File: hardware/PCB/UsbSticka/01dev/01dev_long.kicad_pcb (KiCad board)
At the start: 2 copper layers, 17.7 x 51.8 mm, 22 parts, among them P1 USB_B, P2 MIC, SW1 SW_PUSH, SW2 SW_PUSH, U1 LM1117-3.3, U2 MAX9813, U3 ESP-07v2, U4 MCP3201

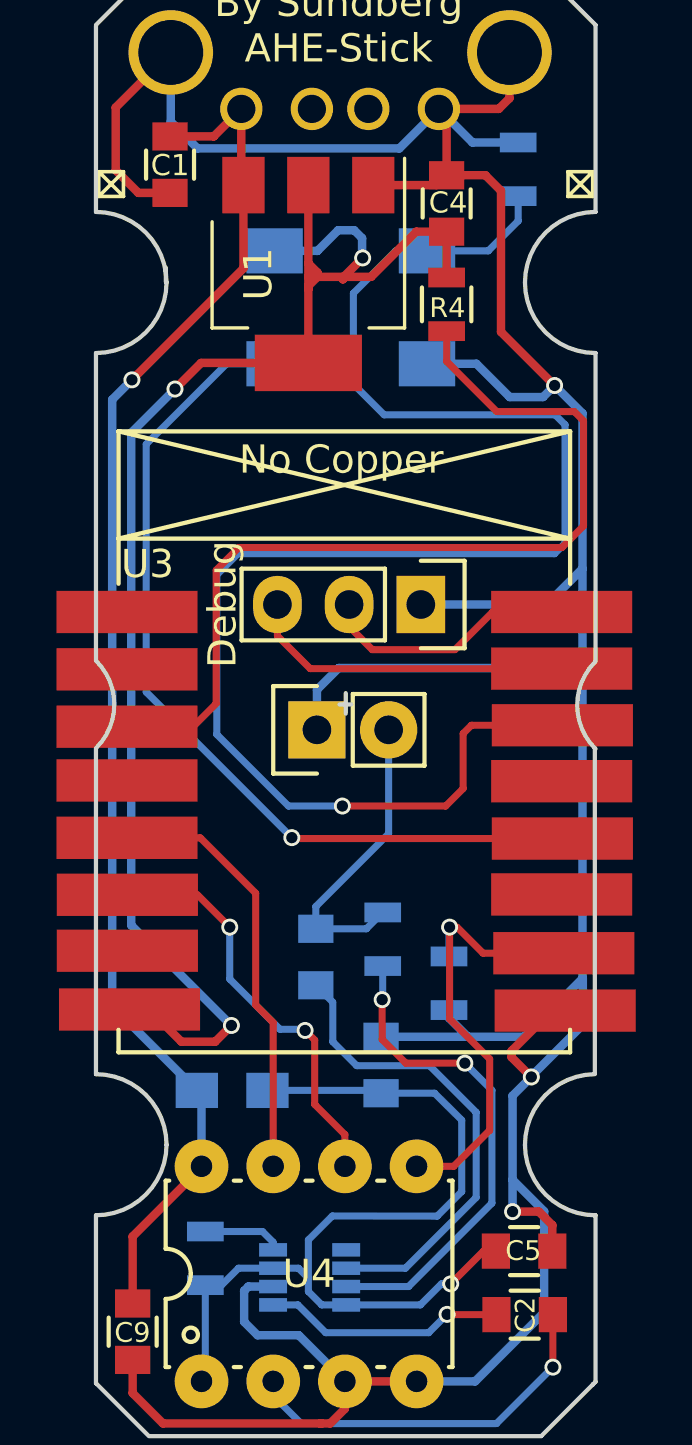
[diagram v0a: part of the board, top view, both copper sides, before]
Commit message: USB Sticka 3D
Dev 06 + 3d modell usb
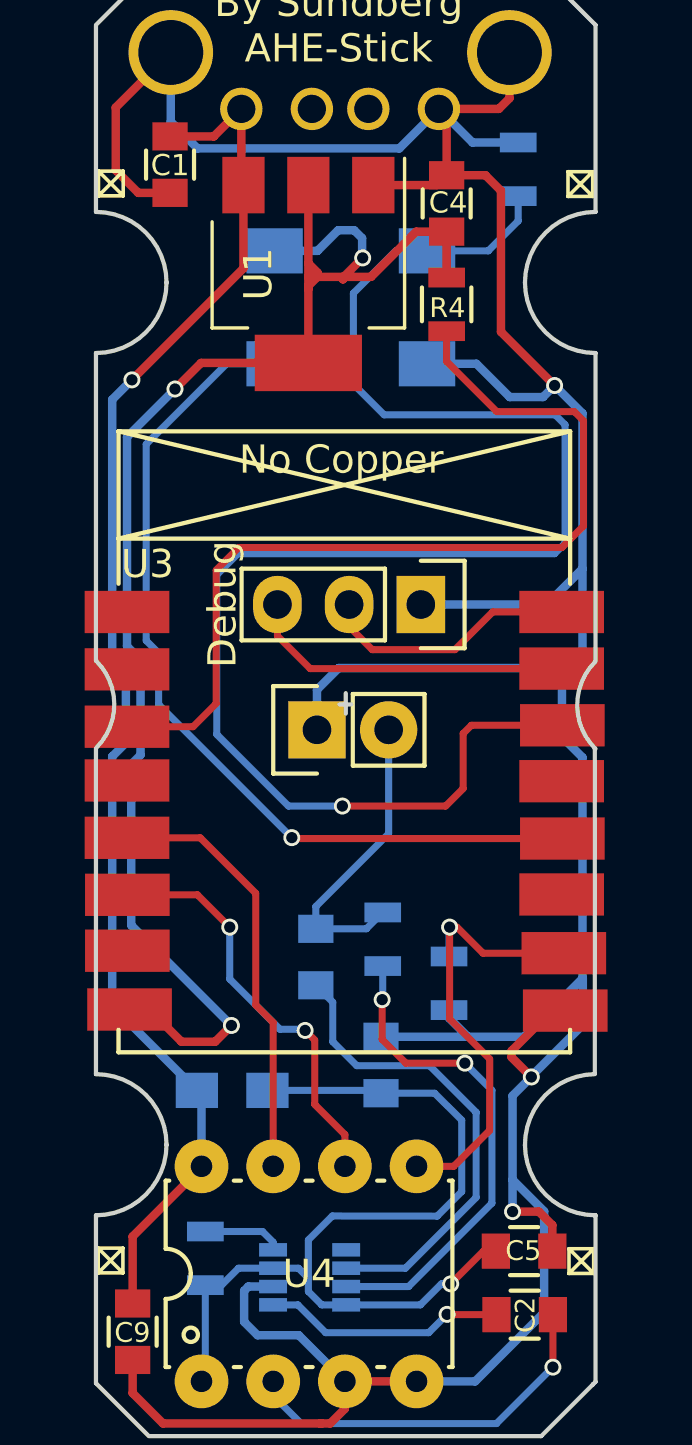
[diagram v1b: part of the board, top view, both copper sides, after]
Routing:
- net GND: track 141.5 -> 142.1 mm
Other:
- outline, holes or cut-outs redrawn

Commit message: MicroUSB
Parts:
- added P1: USB_B, ASKicadLib:USB_A_AS, F.Cu at (0.00, 0.00)
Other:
- board text added: "AHE-Stick"
- board text removed: "By Sundberg AHE-Stick"
